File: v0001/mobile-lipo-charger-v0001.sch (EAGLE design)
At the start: 82 parts, among them IC1 AD8610MR, IC3 AD8610MR, IC5 STM32F429NGH, SW2 DHT-4235A, T1 BC846, T2 BC846, T3 BC846, U3 3.3V, U4 3.3V

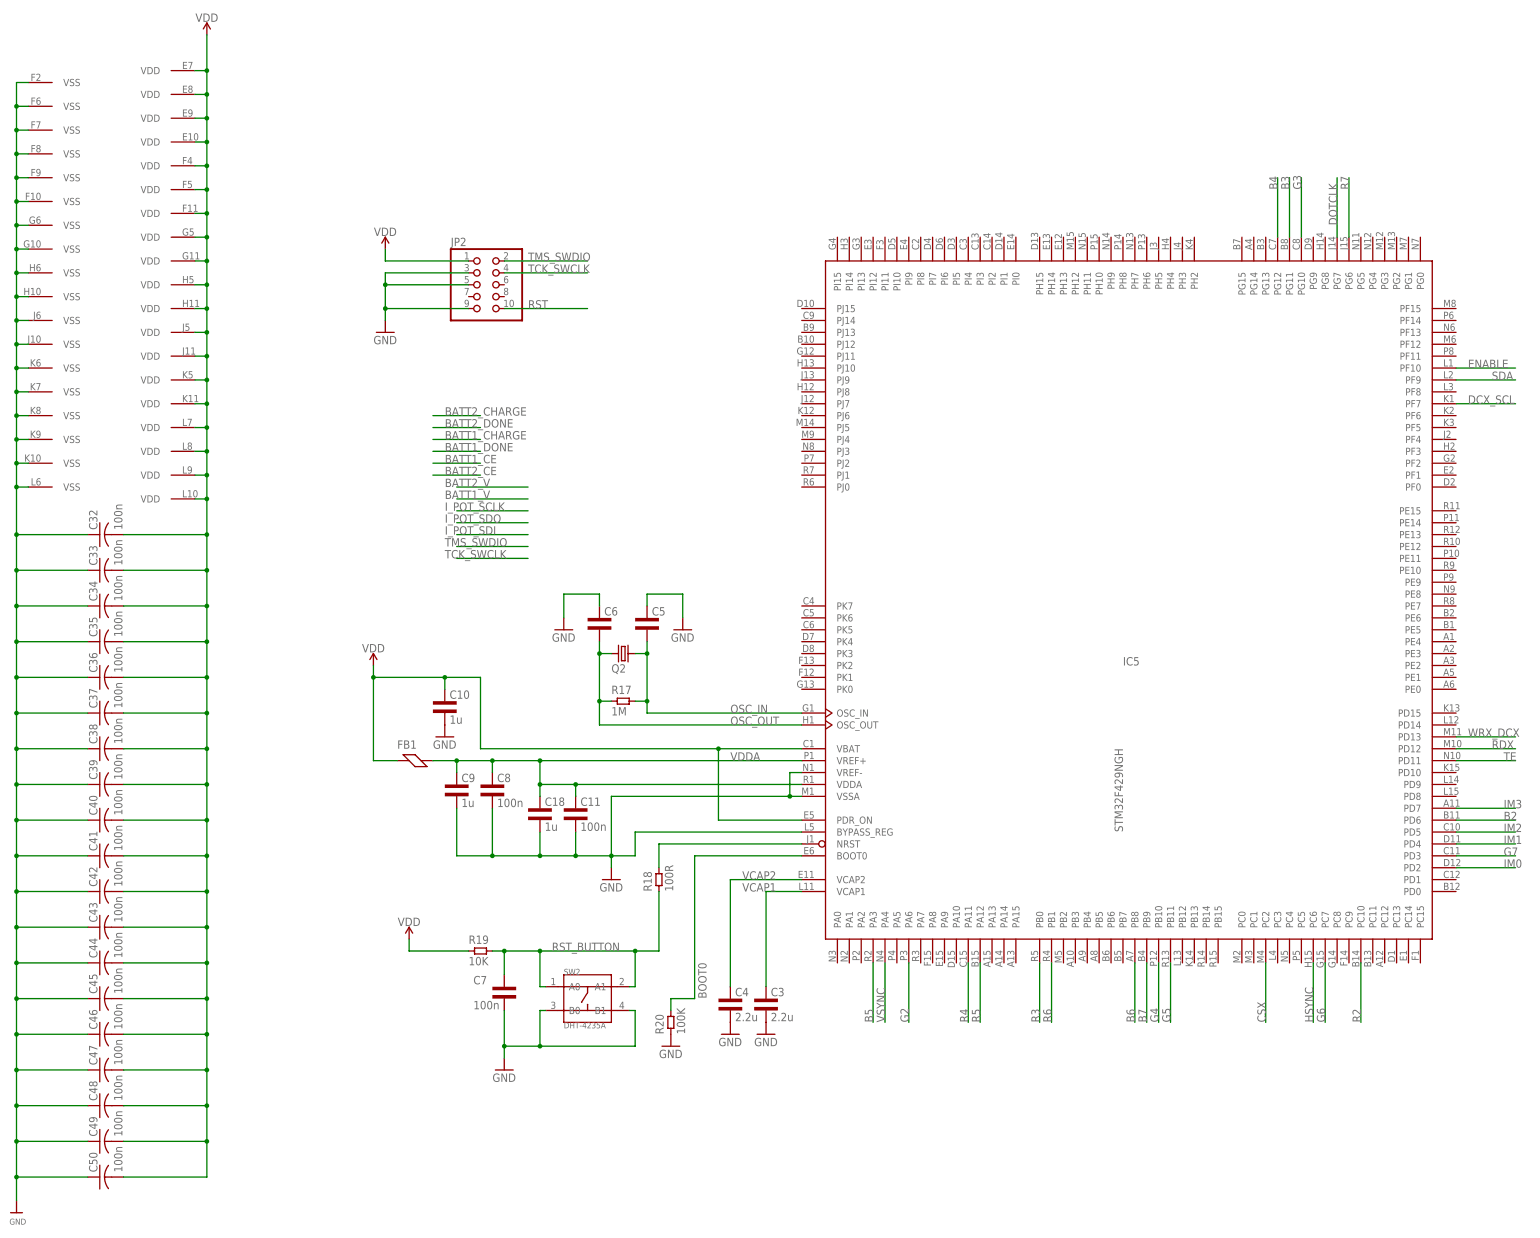
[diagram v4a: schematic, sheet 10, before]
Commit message: TFT Changes
Changed the data lines to the TFT and rerouted some of the charge IC lines
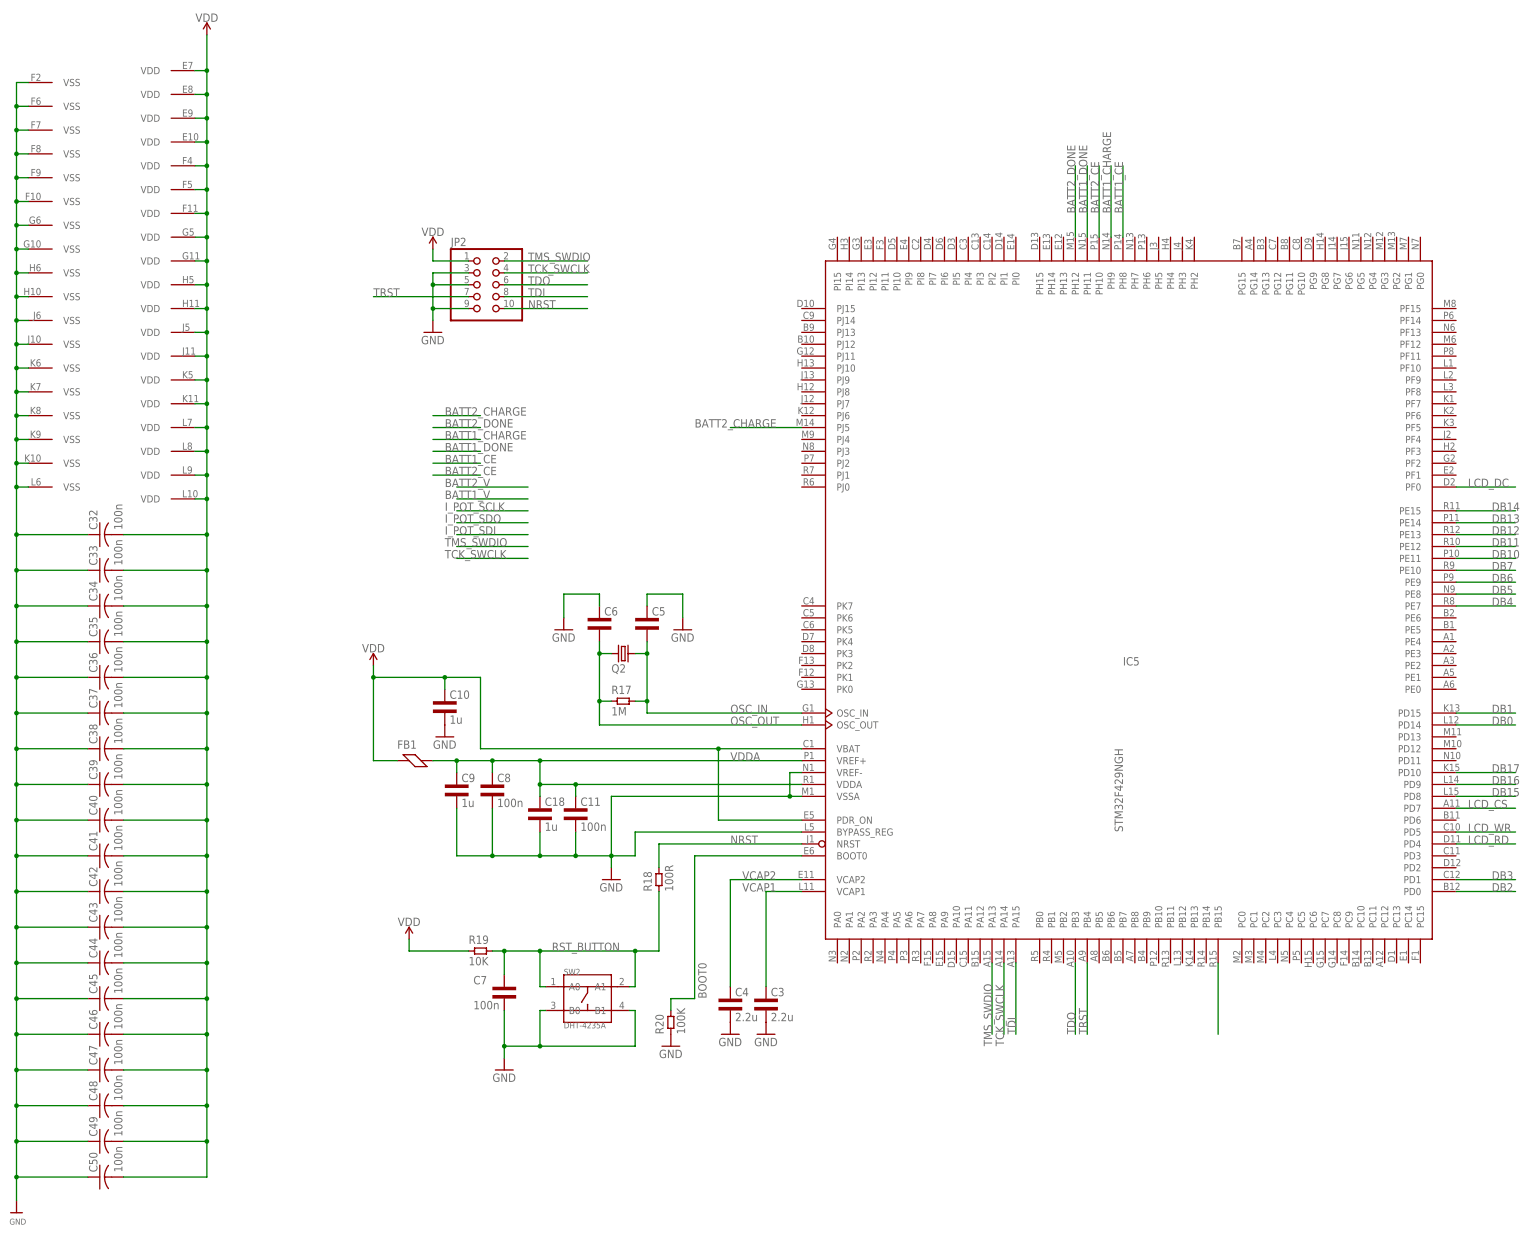
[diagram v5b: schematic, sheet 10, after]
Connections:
- removed net B2: IC5MCU.PD6
- removed net B3: IC5MCU.PG11
- removed net B4: IC5MCU.PG12
- removed net B5: IC5MCU.PA3
- removed net B6: IC5MCU.PB8
- removed net B7: IC5MCU.PB9
- removed net CSX: IC5MCU.PC2, J1.38
- removed net DCX_SCL: IC5MCU.PF7, J1.37
- removed net DOTCLK: IC5MCU.PG7
- removed net G2: IC5MCU.PA6
- removed net G3: IC5MCU.PG10
- removed net G4: IC5MCU.PB10
- removed net G5: IC5MCU.PB11
- removed net G6: IC5MCU.PC7
- removed net G7: IC5MCU.PD3
- removed net HSYNC: IC5MCU.PC6
- removed net IM0: IC5MCU.PD2
- removed net IM1: IC5MCU.PD4
- removed net IM2: IC5MCU.PD5
- removed net IM3: IC5MCU.PD7
- removed net N$3: IC5MCU.NRST, R18.2
- removed net R2: IC5MCU.PC10
- removed net R3: IC5MCU.PB0
- removed net R4: IC5MCU.PA11
- removed net R5: IC5MCU.PA12
- removed net R6: IC5MCU.PB1
- removed net R7: IC5MCU.PG6
- removed net RDX: IC5MCU.PD12
- removed net SDA: IC5MCU.PF9
- removed net TE: IC5MCU.PD11
- removed net TFT_RD#: J1.35
- removed net TFT_WR_RS#: J1.36
- removed net VSYNC: IC5MCU.PA4
- removed net WRX_DCX: IC5MCU.PD13
- new net LCD_CS: IC5MCU.PD7, J1.38
- new net LCD_DC: IC5MCU.PF0, J1.37
- new net LCD_RD: IC5MCU.PD4, J1.35
- new net LCD_WR: IC5MCU.PD5, J1.36
- new net N$12: IC5MCU.PB15
- new net NRST: IC5MCU.NRST, JP2.10, R18.2
- new net TDI: IC5MCU.PA15, JP2.8
- new net TDO: IC5MCU.PB3, JP2.6
- new net TRST: IC5MCU.PB4, JP2.7
- net BATT1_CE: now also IC5MCU.PH8
- net BATT1_CHARGE: now also IC5MCU.PH9
- net BATT1_DONE: now also IC5MCU.PH11
- net BATT2_CE: now also IC5MCU.PH10
- net BATT2_CHARGE: now also IC5MCU.PJ5
- net BATT2_DONE: now also IC5MCU.PH12
- net DB0: now also IC5MCU.PD14
- net DB1: now also IC5MCU.PD15
- net DB10: now also IC5MCU.PE11
- net DB11: now also IC5MCU.PE12
- net DB12: now also IC5MCU.PE13
- net DB13: now also IC5MCU.PE14
- net DB14: now also IC5MCU.PE15
- net DB15: now also IC5MCU.PD8
- net DB16: now also IC5MCU.PD9
- net DB17: now also IC5MCU.PD10
- net DB2: now also IC5MCU.PD0
- net DB3: now also IC5MCU.PD1
- net DB4: now also IC5MCU.PE7
- net DB5: now also IC5MCU.PE8
- net DB6: now also IC5MCU.PE9
- net DB7: now also IC5MCU.PE10
- net ENABLE: no longer IC5MCU.PF10
- net GND: now also J1.11, J1.12, J1.13
- net RST: no longer JP2.10
- net TCK_SWCLK: now also IC5MCU.PA14
- net TMS_SWDIO: now also IC5MCU.PA13

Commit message: TFT Routing
Began routing the TFT connections from the MCU BGA to the FPC
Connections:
- removed net N$12: IC5MCU.PB15
- net BATT1_V: now also IC5MCU.PA1
- net BATT2_V: now also IC5MCU.PA2
- net I_POT_SCLK: now also IC5MCU.PB13
- net I_POT_SDI: now also IC5MCU.PB15
- net I_POT_SDO: now also IC5MCU.PB14
- net VDDA: no longer IC5MCU.VREF+
